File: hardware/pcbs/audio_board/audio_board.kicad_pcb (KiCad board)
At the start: 4 copper layers, 152 x 61.5 mm, 182 parts, among them J1 Conn_02x07_Odd_Even, J2 MTA100_08, J3 NC3MAH, J4 AudioJack3, J5 NC3MAH, J6 NC3FAH1, J7 NC3FAH1, J8 NC3FAH1, J9 AudioJack3, Q1 S8050, Q2 2N7002, Q3 SI2309CDS-T1-GE3, Q4 2N7002, Q5 SI2309CDS-T1-GE3, Q6 2N7002, Q7 SI2309CDS-T1-GE3, U1 Teensy 4.1, U2 LP5907MFX-3.3, U3 LM5158, U4 TAD5242, U5 TAD5242, U6 TAA3040, U7 LMK1C1103A, U8 LMK1C1103A

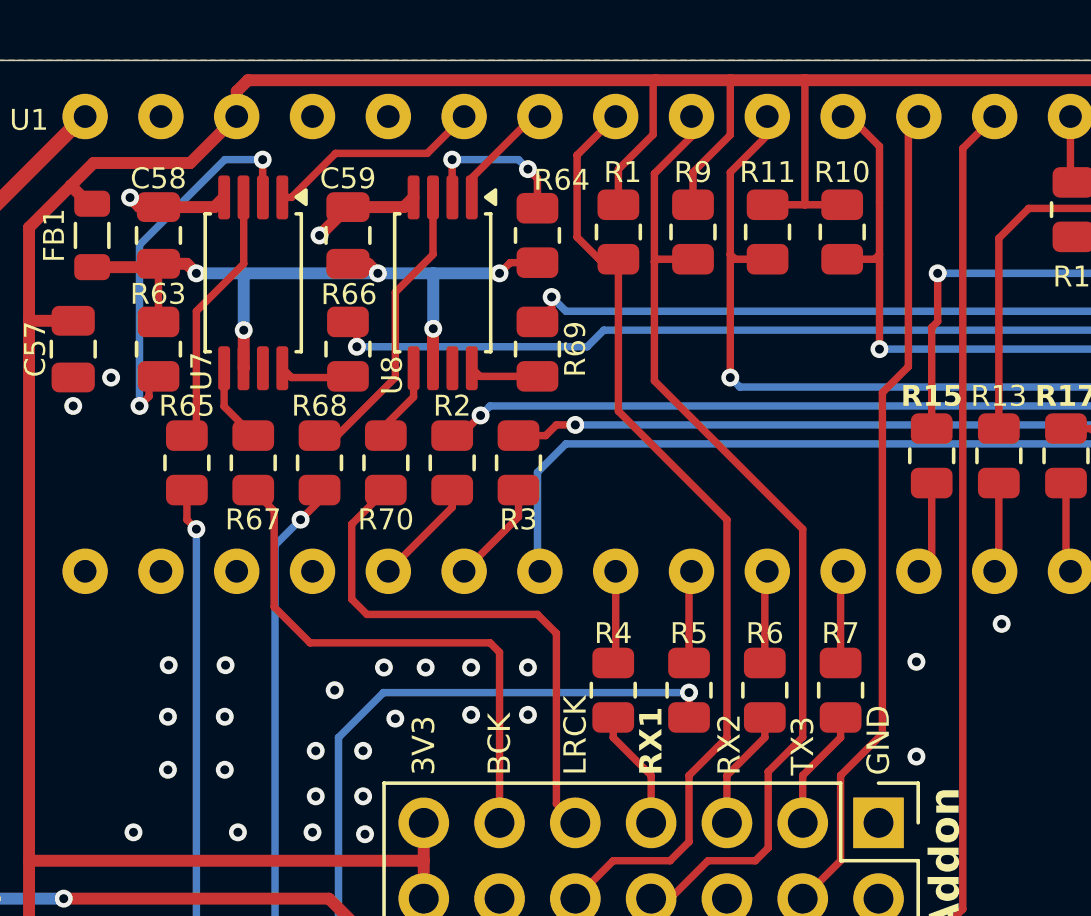
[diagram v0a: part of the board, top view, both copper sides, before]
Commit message: audioboard: add bridges to clock fanout chips
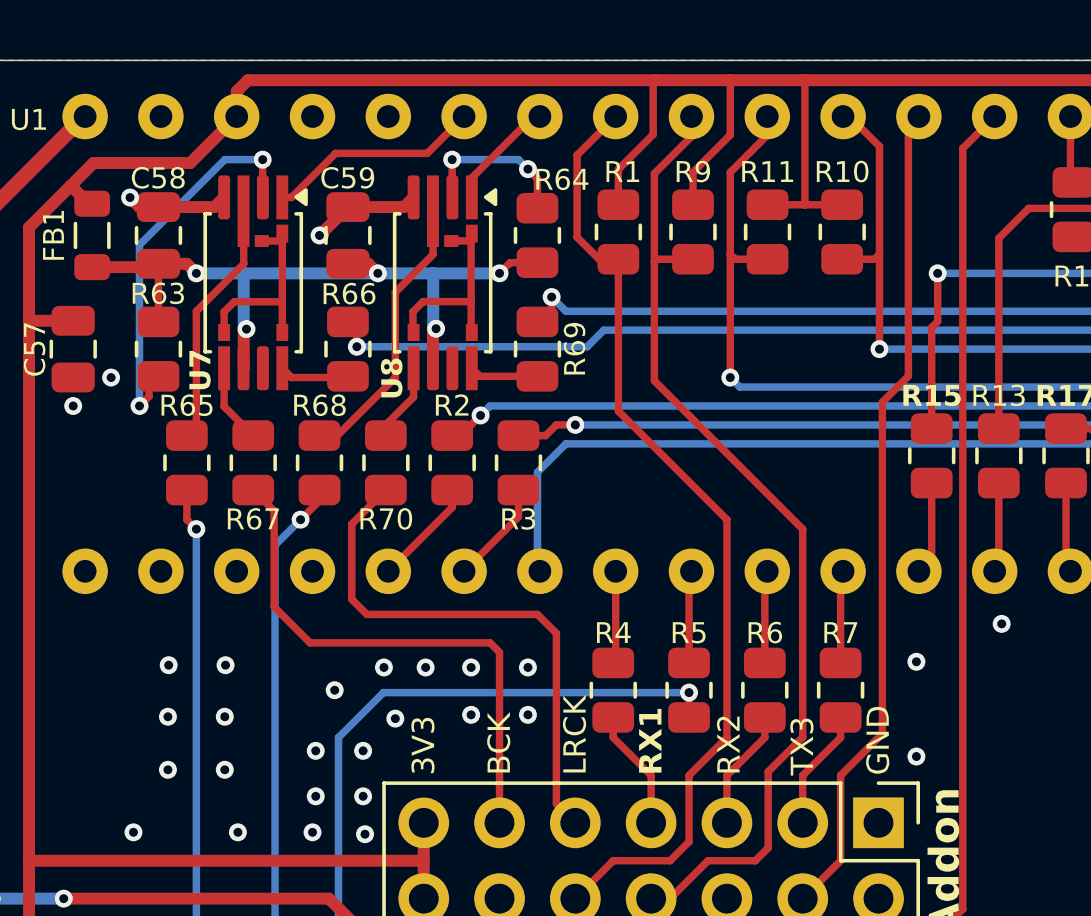
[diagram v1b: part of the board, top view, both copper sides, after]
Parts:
- U7, U8: footprint Package_SO:TSSOP-8_4.4x3mm_P0.65mm -> ics:TSSOP-8_4.4x3mm_P0.65mm_bridges
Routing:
- net /Clock fanout/BRIDGE_CA: track 0.00 -> 6.99 mm
- net /Clock fanout/BRIDGE_CB: track 0.00 -> 6.99 mm

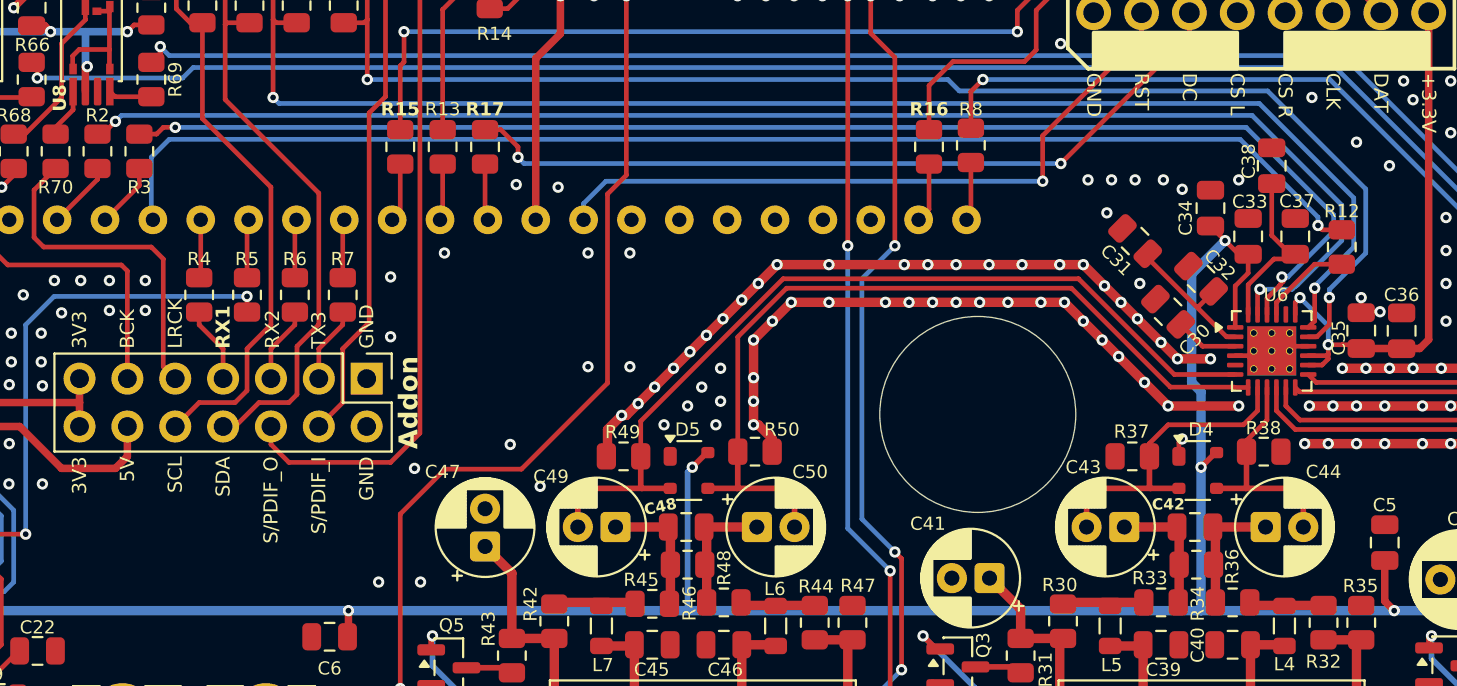
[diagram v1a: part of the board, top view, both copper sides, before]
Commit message: audioboard: minor layout improvements
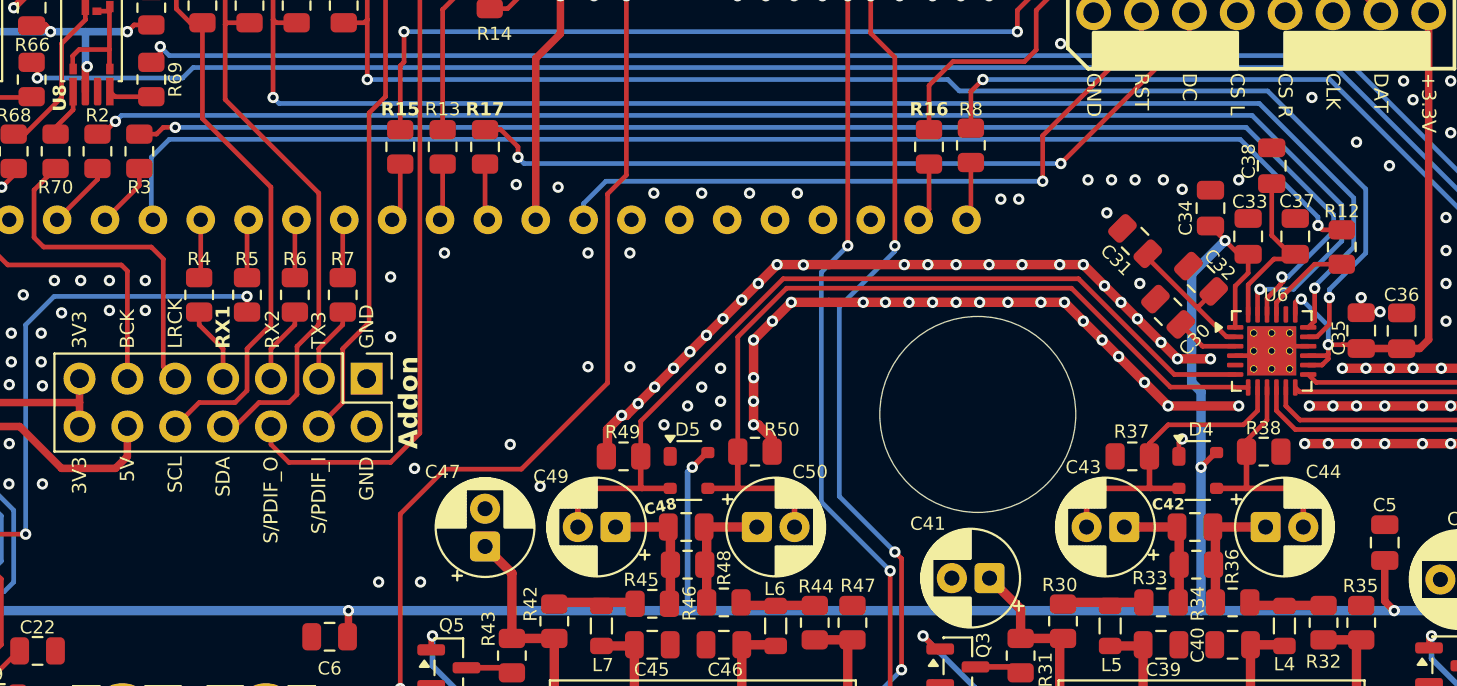
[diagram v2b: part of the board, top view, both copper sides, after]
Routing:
- net /PHANTOM_IN2_EN: track 50.4 -> 51.6 mm
- net /PHANTOM_IN3_EN: track 89.6 -> 90.6 mm
- net GND: vias 285 -> 291
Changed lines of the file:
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@@
 	)
 	(via
-		(at 145.5 110.25)
+		(at 147.32 110.25)
 		(size 0.6)
 		(drill 0.3)
@@
 	)
 	(via
+		(at 136.2075 104.4575)
+		(size 0.6)
+		(drill 0.3)
+		(layers "F.Cu" "B.Cu")
+		(free yes)
+		(net "GND")
+	)
+	(via
 		(at 153 134.25)
 		(size 0.6)
@@
 	)
 	(via
+		(at 144.145 108.2675)
+		(size 0.6)
+		(drill 0.3)
+		(layers "F.Cu" "B.Cu")
+		(capping no)
+		(covering
+			(front no)
+			(back no)
+		)
+		(plugging
+			(front no)
+			(back no)
+		)
+		(filling no)
+		(net "GND")
+	)
+	(via
 		(at 90.411094 108)
 		(size 0.6)
@@
 	)
 	(via
+		(at 141.2875 104.4575)
+		(size 0.6)
+		(drill 0.3)
+		(layers "F.Cu" "B.Cu")
+		(free yes)
+		(net "GND")
+	)
+	(via
 		(at 100.33 123.5075)
 		(size 0.6)
@@
 	)
 	(via
+		(at 143.8275 104.4575)
+		(size 0.6)
+		(drill 0.3)
+		(layers "F.Cu" "B.Cu")
+		(free yes)
+		(net "GND")
+	)
+	(via
 		(at 128.905 104)
 		(size 0.6)
@@
 	)
 	(via
+		(at 155.575 104.775)
+		(size 0.6)
+		(drill 0.3)
+		(layers "F.Cu" "B.Cu")
+		(free yes)
+		(net "GND")
+	)
+	(via
 		(at 103.759 119.888)
 		(size 0.6)
@@
 	)
 	(via
+		(at 154.6225 104.775)
+		(size 0.6)
+		(drill 0.3)
+		(layers "F.Cu" "B.Cu")
+		(free yes)
+		(net "GND")
+	)
+	(via
 		(at 179.5 113.75)
 		(size 0.6)
@@
 	)
 	(via
-		(at 145.5 108.25)
+		(at 131.1275 104.14)
 		(size 0.6)
 		(drill 0.3)
 		(layers "F.Cu" "B.Cu")
+		(free yes)
 		(capping no)
 		(covering
@@
 	)
 	(via
-		(at 131.1275 104.14)
+		(at 138.7475 104.4575)
 		(size 0.6)
 		(drill 0.3)
 		(layers "F.Cu" "B.Cu")
 		(free yes)
-		(capping no)
-		(covering
-			(front no)
-			(back no)
-		)
-		(plugging
-			(front no)
-			(back no)
-		)
-		(filling no)
 		(net "GND")
 	)
@@
 	)
 	(segment
-		(start 170.25 110.893261)
-		(end 170.25 110.25)
-		(width 0.25)
-		(layer "F.Cu")
-		(net "+3.3V")
-	)
-	(segment
 		(start 177.33 94.88)
 		(end 177.33 112.23)
@@
 	)
 	(segment
+		(start 170.419208 110.080792)
+		(end 170.25 110.25)
+		(width 0.25)
+		(layer "F.Cu")
+		(net "+3.3V")
+	)
+	(segment
 		(start 131.25 93.98)
 		(end 131.25 96)
@@
 	)
 	(segment
-		(start 170.25 110.25)
-		(end 170.5 110)
-		(width 0.25)
-		(layer "F.Cu")
-		(net "+3.3V")
-	)
-	(segment
 		(start 170.9375 113.080761)
 		(end 171.919239 113.080761)
@@
 	)
 	(segment
+		(start 170.25 110.25)
+		(end 170.25 110.893261)
+		(width 0.25)
+		(layer "F.Cu")
+		(net "+3.3V")
+	)
+	(segment
 		(start 94.66125 92.1875)
 		(end 93.900625 92.948125)
@@
 		(net "+3.3V")
 	)
+	(segment
+		(start 170.568532 110.080792)
+		(end 170.419208 110.080792)
+		(width 0.25)
+		(layer "F.Cu")
+		(net "+3.3V")
+	)
 	(via
 		(at 172 112.5)
@@
 	)
 	(via
-		(at 170.5 110)
+		(at 170.568532 110.080792)
 		(size 0.6)
 		(drill 0.3)
@@
 	)
 	(segment
-		(start 170.5 110)
+		(start 170.580792 110.080792)
 		(end 172 111.5)
 		(width 0.25)
@@
 	)
 	(segment
+		(start 170.568532 110.080792)
+		(end 170.580792 110.080792)
+		(width 0.25)
+		(layer "B.Cu")
+		(net "+3.3V")
+	)
+	(segment
 		(start 113.9825 115.57)
 		(end 114.6175 114.935)
@@
 	)
 	(segment
-		(start 172.72 105.0925)
-		(end 167.9575 100.33)
+		(start 168.371669 109.554169)
+		(end 170.163331 109.554169)
 		(width 0.25)
 		(layer "B.Cu")
@@
 	)
 	(segment
-		(start 172.72 106.972026)
-		(end 172.72 105.0925)
+		(start 172.72 105.0925)
+		(end 167.9575 100.33)
 		(width 0.25)
 		(layer "B.Cu")
@@
 	)
 	(segment
-		(start 107.6325 100.6475)
+		(start 167.9575 100.33)
 		(end 107.95 100.33)
 		(width 0.25)
@@
 	)
 	(segment
-		(start 170.353105 109.338921)
-		(end 172.72 106.972026)
-		(width 0.25)
-		(layer "B.Cu")
-		(net "/I2S2_FS")
-	)
-	(segment
-		(start 170.248986 109.394)
-		(end 170.27451 109.394)
-		(width 0.25)
-		(layer "B.Cu")
-		(net "/I2S2_FS")
-	)
-	(segment
-		(start 170.329589 109.338921)
-		(end 170.353105 109.338921)
-		(width 0.25)
-		(layer "B.Cu")
-		(net "/I2S2_FS")
-	)
-	(segment
-		(start 170.27451 109.394)
-		(end 170.329589 109.338921)
-		(width 0.25)
-		(layer "B.Cu")
-		(net "/I2S2_FS")
-	)
-	(segment
-		(start 167.9575 100.33)
-		(end 107.95 100.33)
+		(start 172.72 106.9975)
+		(end 172.72 105.0925)
 		(width 0.25)
 		(layer "B.Cu")
@@
 	)
 	(segment
-		(start 170.088817 109.554169)
-		(end 170.248986 109.394)
+		(start 170.163331 109.554169)
+		(end 172.72 106.9975)
 		(width 0.25)
 		(layer "B.Cu")
@@
 	)
 	(segment
-		(start 168.371669 109.554169)
-		(end 170.088817 109.554169)
+		(start 107.95 100.33)
+		(end 107.6325 100.6475)
 		(width 0.25)
 		(layer "B.Cu")
@@
 	)
 	(segment
-		(start 146.5 107.25)
-		(end 146.5 122.25)
-		(width 0.25)
-		(layer "B.Cu")
-		(net "/PHANTOM_IN2_EN")
-	)
-	(segment
 		(start 148.75 132.3)
 		(end 152.6125 136.1625)
@@
 	)
 	(segment
-		(start 146.5 122.25)
-		(end 148.75 124.5)
+		(start 145.0975 108.6525)
+		(end 145.0975 120.8475)
 		(width 0.25)
 		(layer "B.Cu")
@@
 	)
 	(segment
+		(start 146.5 107.25)
+		(end 145.0975 108.6525)
+		(width 0.25)
+		(layer "B.Cu")
+		(net "/PHANTOM_IN2_EN")
+	)
+	(segment
+		(start 145.0975 120.8475)
+		(end 148.75 124.5)
+		(width 0.25)
+		(layer "B.Cu")
+		(net "/PHANTOM_IN2_EN")
+	)
+	(segment
 		(start 191.8375 116.5)
 		(end 193.5875 118.25)
@@
 	)
 	(segment
-		(start 147.25 121.75)
-		(end 147.25 109)
-		(width 0.25)
-		(layer "B.Cu")
-		(net "/PHANTOM_IN3_EN")
-	)
-	(segment
-		(start 149 123.5)
-		(end 147.25 121.75)
+		(start 146.05 110.49)
+		(end 149 107.54)
 		(width 0.25)
 		(layer "B.Cu")
@@
 	)
 	(segment
-		(start 149.355 129.75)
-		(end 147.969997 131.135003)
+		(start 149 123.5)
+		(end 146.05 120.55)
 		(width 0.25)
 		(layer "B.Cu")
@@
 	)
 	(segment
-		(start 147.25 109)
+		(start 149 107.54)
 		(end 149 107.25)
 		(width 0.25)
@@
 	)
 	(segment
+		(start 149.355 129.75)
+		(end 147.969997 131.135003)
+		(width 0.25)
+		(layer "B.Cu")
+		(net "/PHANTOM_IN3_EN")
+	)
+	(segment
 		(start 178.25 136.1875)
 		(end 174.7625 136.1875)
 		(width 0.25)
 		(layer "B.Cu")
+		(net "/PHANTOM_IN3_EN")
+	)
+	(segment
+		(start 146.05 120.55)
+		(end 146.05 110.49)
+		(width 0.25)
+		(layer "B.Cu")

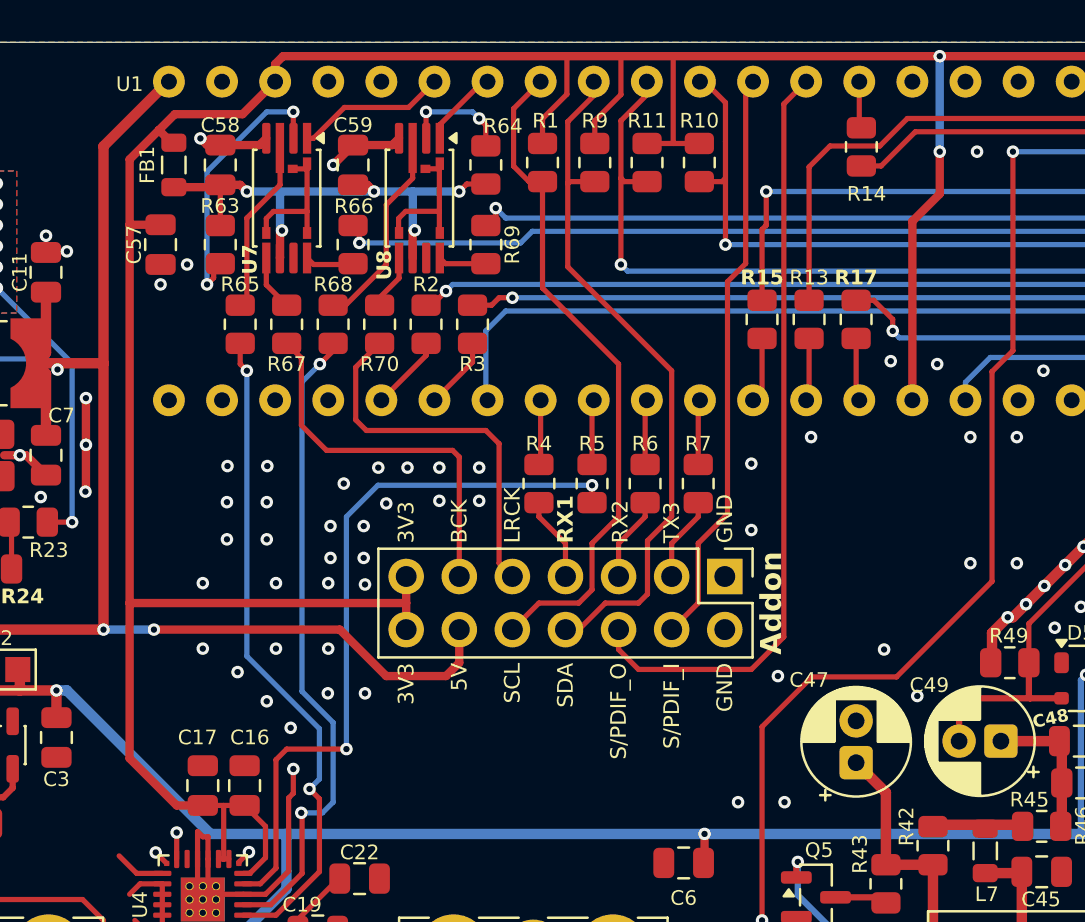
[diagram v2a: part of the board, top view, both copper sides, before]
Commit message: rearrange addon header
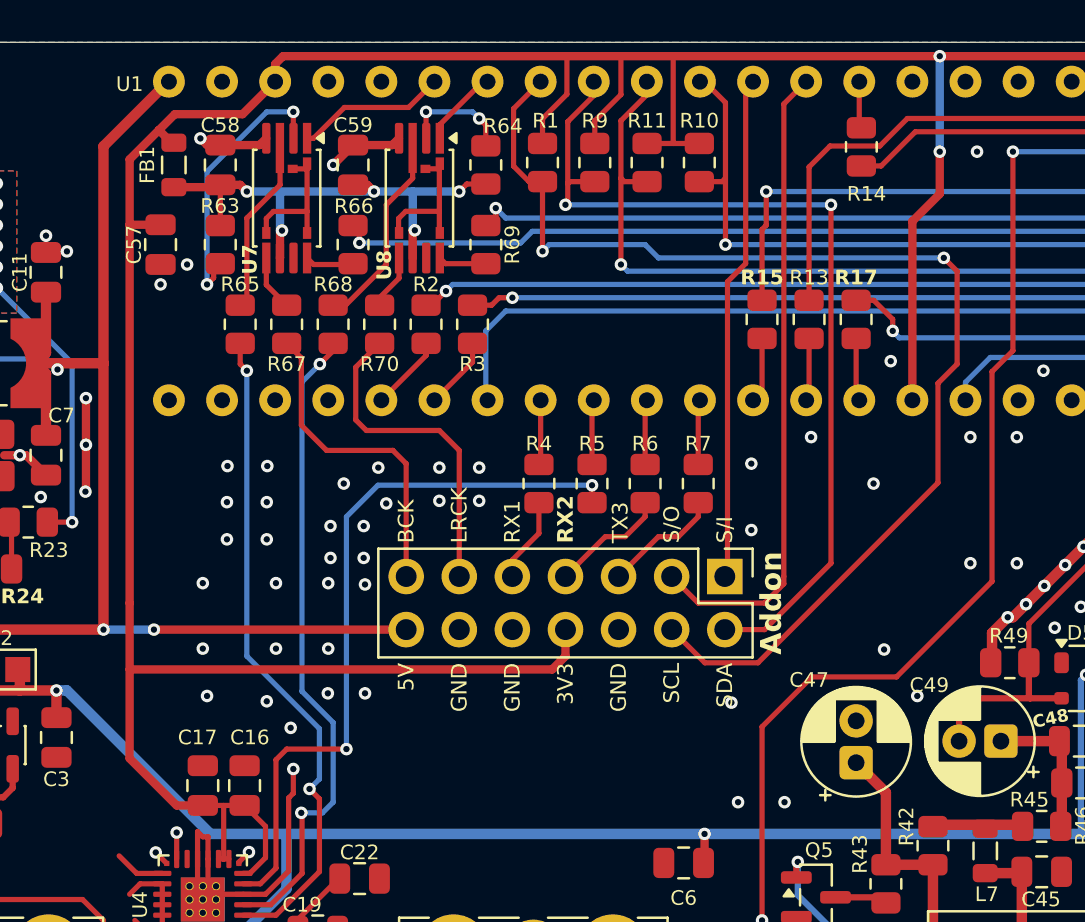
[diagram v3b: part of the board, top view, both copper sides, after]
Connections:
- J1 pad 1: GND -> /SPDIF_IN
- J1 pad 10: /SCL -> GND
- J1 pad 11: /I2S1_BCLK -> /I2S1_LRCLK
- J1 pad 12: +5V -> GND
- J1 pad 13: +3.3V -> /I2S1_BCLK
- J1 pad 14: +3.3V -> +5V
- J1 pad 2: GND -> /SDA
- J1 pad 3: /I2S1_TX3 -> /SPDIF_OUT
- J1 pad 4: /SPDIF_IN -> /SCL
- J1 pad 5: Net-(J1-Pin_5) -> /I2S1_TX3
- J1 pad 6: /SPDIF_OUT -> GND
- J1 pad 8: /SDA -> +3.3V
- J1 pad 9: /I2S1_LRCLK -> Net-(J1-Pin_9-Pad9)
- R4 pad 2: Net-(J1-Pin_7) -> Net-(J1-Pin_9-Pad9)
- R6 pad 2: Net-(J1-Pin_5) -> Net-(J1-Pin_7)
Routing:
- net /SCL: track 32.6 -> 57.7 mm, vias 0 -> 2
- net /SDA: track 33.5 -> 44.1 mm, vias 0 -> 2
- net +3.3V: track 300.0 -> 307.2 mm
- net /SPDIF_OUT: track 36.9 -> 30.7 mm
- net +5V: track 101.2 -> 95.9 mm
- net Net-(J1-Pin_9-Pad9): track 0.00 -> 4.06 mm
- net Net-(J1-Pin_5): track 4.06 -> 0.00 mm
- net /SPDIF_IN: track 27.8 -> 24.2 mm
- net /I2S1_BCLK: track 18.1 -> 15.4 mm
- net /I2S1_LRCLK: track 18.1 -> 15.7 mm
- net Net-(J1-Pin_7): track 4.06 -> 5.67 mm
- net /I2S1_TX3: track 4.06 -> 5.67 mm
- net GND: vias 291 -> 290
